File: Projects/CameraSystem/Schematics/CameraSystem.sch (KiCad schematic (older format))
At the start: 0 parts

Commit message: feat: add debugging pins
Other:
- note added: "To be done:\n1. Add debug ping in all communication lines"
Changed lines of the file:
@@
 Wire Wire Line
 	3350 5300 1750 5300
+Text Notes 8900 1650 0    60   ~ 0
+To be done:\n1. Add debug ping in all communication lines
 $EndSCHEMATC

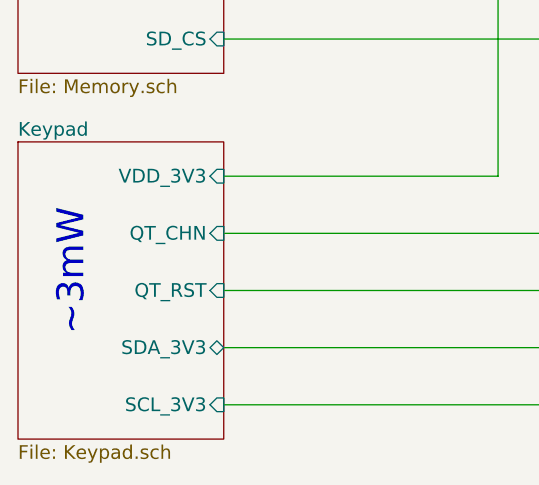
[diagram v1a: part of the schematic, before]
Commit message: feat: add interface to Q Pad
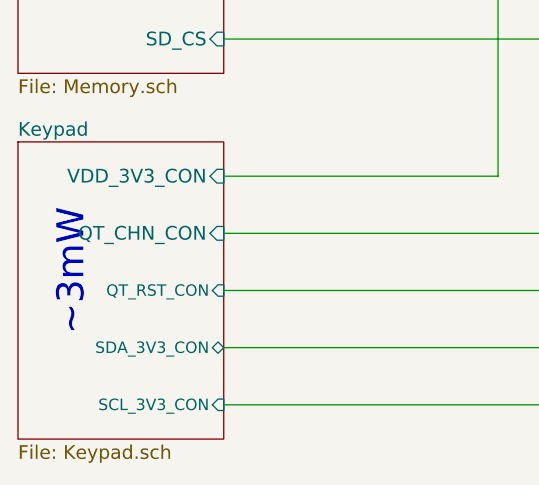
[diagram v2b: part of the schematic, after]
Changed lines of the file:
@@
 F0 "Keypad" 60
 F1 "Keypad.sch" 60
-F2 "VDD_3V3" I R 1750 6400 60
-F3 "SDA_3V3" B R 1750 7150 60
-F4 "SCL_3V3" I R 1750 7400 60
-F5 "QT_RST" I R 1750 6900 60
-F6 "QT_CHN" I R 1750 6650 60
+F2 "QT_RST_CON" I R 1750 6900 50
+F3 "QT_CHN_CON" I R 1750 6650 60
+F4 "SCL_3V3_CON" I R 1750 7400 50
+F5 "SDA_3V3_CON" B R 1750 7150 50
+F6 "VDD_3V3_CON" I R 1750 6400 60
 $EndSheet
 Wire Wire Line

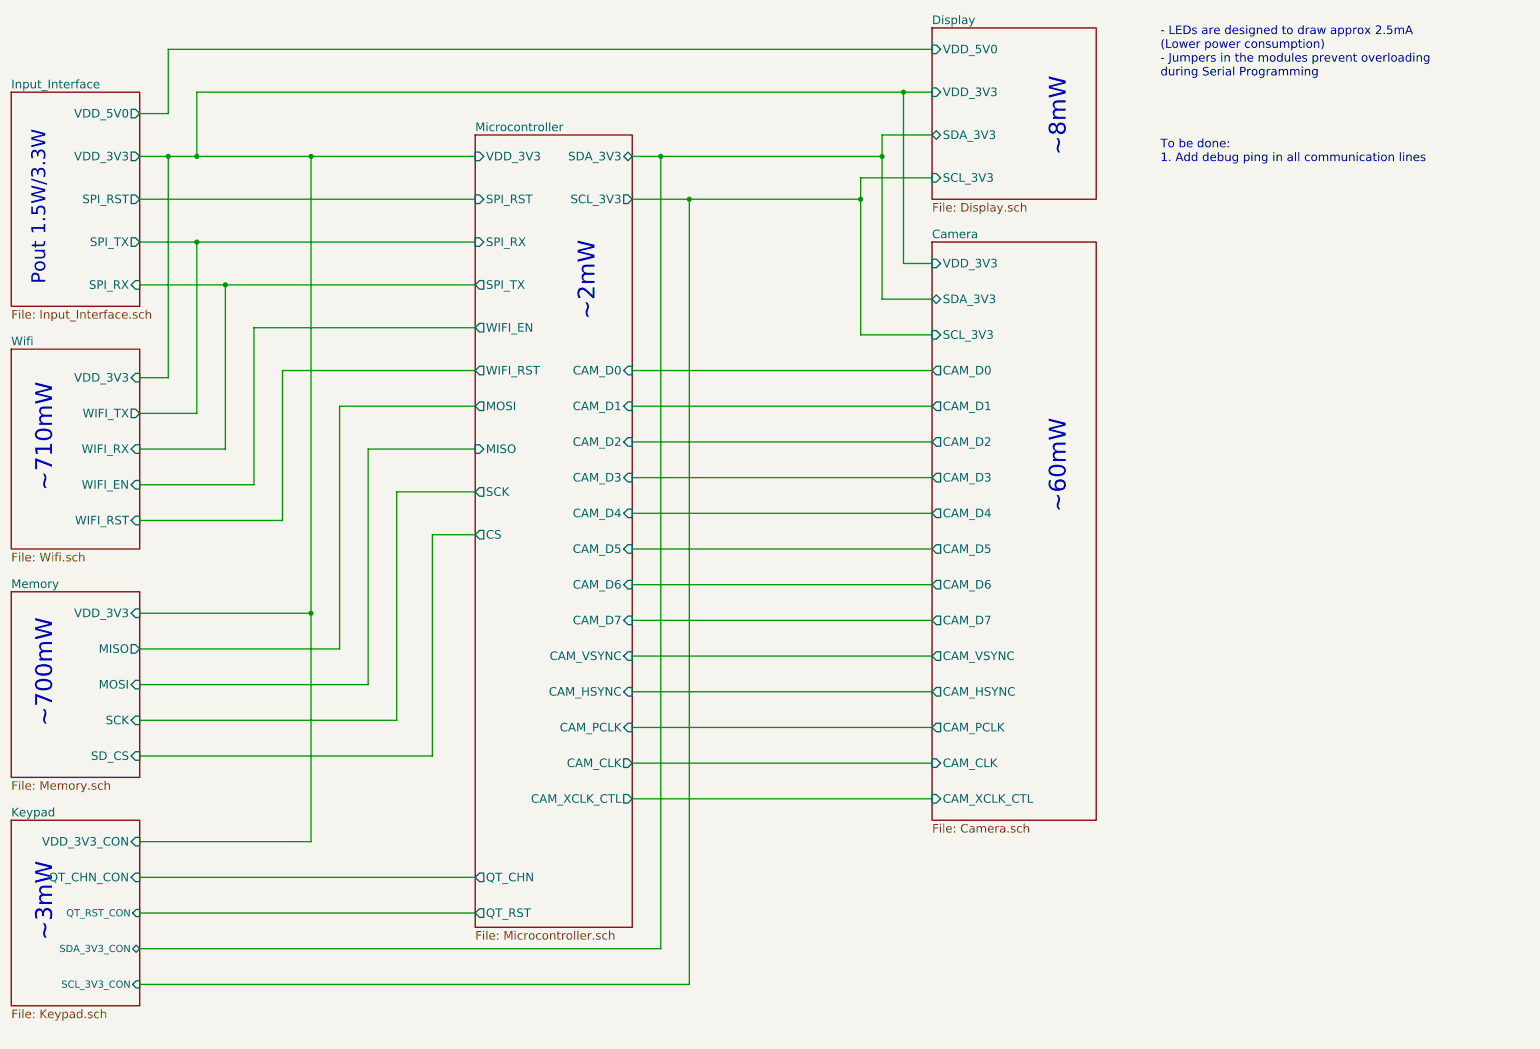
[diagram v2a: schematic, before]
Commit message: feat: add new motor module to the schematic
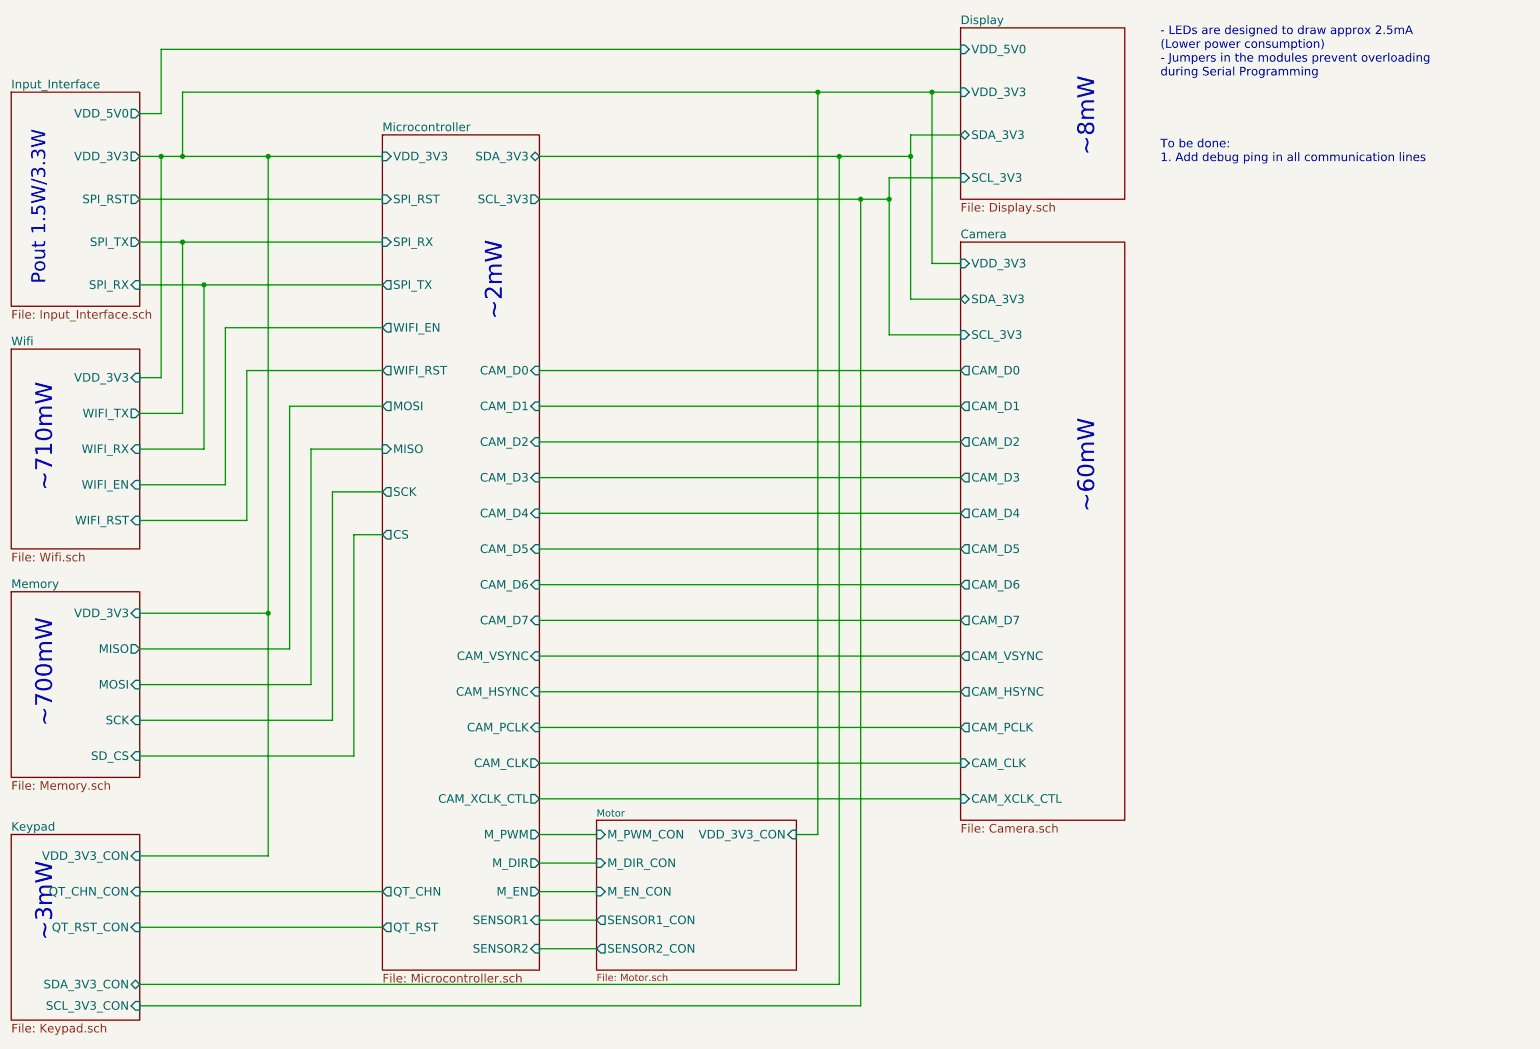
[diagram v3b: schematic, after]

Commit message: feat: assign footprints
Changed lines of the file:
@@
 F32 "SENSOR1" I R 4550 6950 60
 F33 "SENSOR2" I R 4550 7150 60
+F34 "_SD_DET" I L 3450 6000 60
 $EndSheet
 $Sheet
@@
 F5 "WIFI_RST" I R 1750 4150 60
 F6 "WIFI_EN" I R 1750 3900 60
-$EndSheet
-$Sheet
-S 850  4650 900  1300
-U 5BB4DA56
-F0 "Memory" 60
-F1 "Memory.sch" 60
-F2 "VDD_3V3" I R 1750 4800 60
-F3 "MOSI" I R 1750 5300 60
-F4 "SCK" I R 1750 5550 60
-F5 "SD_CS" I R 1750 5800 60
-F6 "MISO" O R 1750 5050 60
 $EndSheet
 $Sheet
@@
 Wire Wire Line
 	6500 1150 7300 1150
+$Sheet
+S 850  4650 900  1450
+U 5BB4DA56
+F0 "Memory" 60
+F1 "Memory.sch" 60
+F2 "VDD_3V3" I R 1750 4800 60
+F3 "MOSI" I R 1750 5300 60
+F4 "SCK" I R 1750 5550 60
+F5 "SD_CS" I R 1750 5800 60
+F6 "MISO" O R 1750 5050 60
+F7 "_SD_DET" O R 1750 6000 60
+$EndSheet
+Wire Wire Line
+	1750 6000 3450 6000
 $EndSCHEMATC

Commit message: feat: layout updated
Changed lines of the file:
@@
 F1 "Memory.sch" 60
 F2 "VDD_3V3" I R 1750 4800 60
-F3 "MOSI" I R 1750 5300 60
-F4 "SCK" I R 1750 5550 60
-F5 "SD_CS" I R 1750 5800 60
-F6 "MISO" O R 1750 5050 60
-F7 "_SD_DET" O R 1750 6000 60
+F3 "SD_CS" I R 1750 5800 60
+F4 "_SD_DET" O R 1750 6000 60
+F5 "SD_MISO" I R 1750 5050 60
+F6 "SD_SCK" I R 1750 5550 60
+F7 "SD_MOSI" O R 1750 5300 60
 $EndSheet
 Wire Wire Line

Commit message: feat: update gerber files
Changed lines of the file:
@@
 F3 "VDD_3V3" O R 1750 1600 60
 F4 "SPI_RST" O R 1750 1900 60
-F5 "SPI_TX" O R 1750 2200 60
-F6 "SPI_RX" I R 1750 2500 60
+F5 "U2U_SPI_TX" O R 1750 2200 60
+F6 "U2U_SPI_RX" I R 1750 2500 60
 $EndSheet
 $Sheet

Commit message: Camera System QT Pad schematic reviewed
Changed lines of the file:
@@
 F25 "CAM_VSYNC" I R 4550 5100 60
 F26 "CAM_XCLK_CTL" O R 4550 6100 60
-F27 "QT_CHN" O L 3450 6750 60
-F28 "QT_RST" O L 3450 7000 60
-F29 "M_PWM" O R 4550 6350 60
-F30 "M_DIR" O R 4550 6550 60
-F31 "M_EN" O R 4550 6750 60
-F32 "SENSOR1" I R 4550 6950 60
-F33 "SENSOR2" I R 4550 7150 60
-F34 "_SD_DET" I L 3450 6000 60
+F27 "QT_RST" O L 3450 7000 60
+F28 "M_PWM" O R 4550 6350 60
+F29 "M_DIR" O R 4550 6550 60
+F30 "M_EN" O R 4550 6750 60
+F31 "SENSOR1" I R 4550 6950 60
+F32 "SENSOR2" I R 4550 7150 60
+F33 "_SD_DET" I L 3450 6000 60
+F34 "QT_CHN" I L 3450 6750 60
 $EndSheet
 $Sheet
@@
 F1 "Keypad.sch" 60
 F2 "QT_RST_CON" I R 1750 7000 60
-F3 "QT_CHN_CON" I R 1750 6750 60
-F4 "SCL_3V3_CON" I R 1750 7550 60
-F5 "SDA_3V3_CON" B R 1750 7400 60
-F6 "VDD_3V3_CON" I R 1750 6500 60
+F3 "SCL_3V3_CON" I R 1750 7550 60
+F4 "SDA_3V3_CON" B R 1750 7400 60
+F5 "VDD_3V3_CON" I R 1750 6500 60
+F6 "QT_CHN_CON" O R 1750 6750 60
 $EndSheet
 Wire Wire Line
@@
 F1 "Memory.sch" 60
 F2 "VDD_3V3" I R 1750 4800 60
-F3 "SD_CS" I R 1750 5800 60
-F4 "_SD_DET" O R 1750 6000 60
-F5 "SD_MISO" I R 1750 5050 60
-F6 "SD_SCK" I R 1750 5550 60
-F7 "SD_MOSI" O R 1750 5300 60
-$EndSheet
-Wire Wire Line
+F3 "_SD_DET" O R 1750 6000 60
+F4 "SD_MISO" I R 1750 5050 60
+F5 "SD_SCK" I R 1750 5550 60
+F6 "SD_MOSI" O R 1750 5300 60
+F7 "_SD_CS" I R 1750 5800 60
+$EndSheet
+Wire Wire Line
